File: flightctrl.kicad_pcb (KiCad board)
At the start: 1 copper layers, 51 parts, among them J1 USB_OTG, SW1 SW_SPST, SW10 ROTARY_ENCODER_SWITCH, SW2 SW_SPST, SW3 SW_SPST, SW4 SW_SPST, SW5 SW_SPDT_MSM, SW6 ROTARY_ENCODER_SWITCH, SW7 ROTARY_ENCODER_SWITCH, SW8 ROTARY_ENCODER_SWITCH, SW9 ROTARY_ENCODER_SWITCH, U1 ATMEGA328P-AU, Y1 12MHz

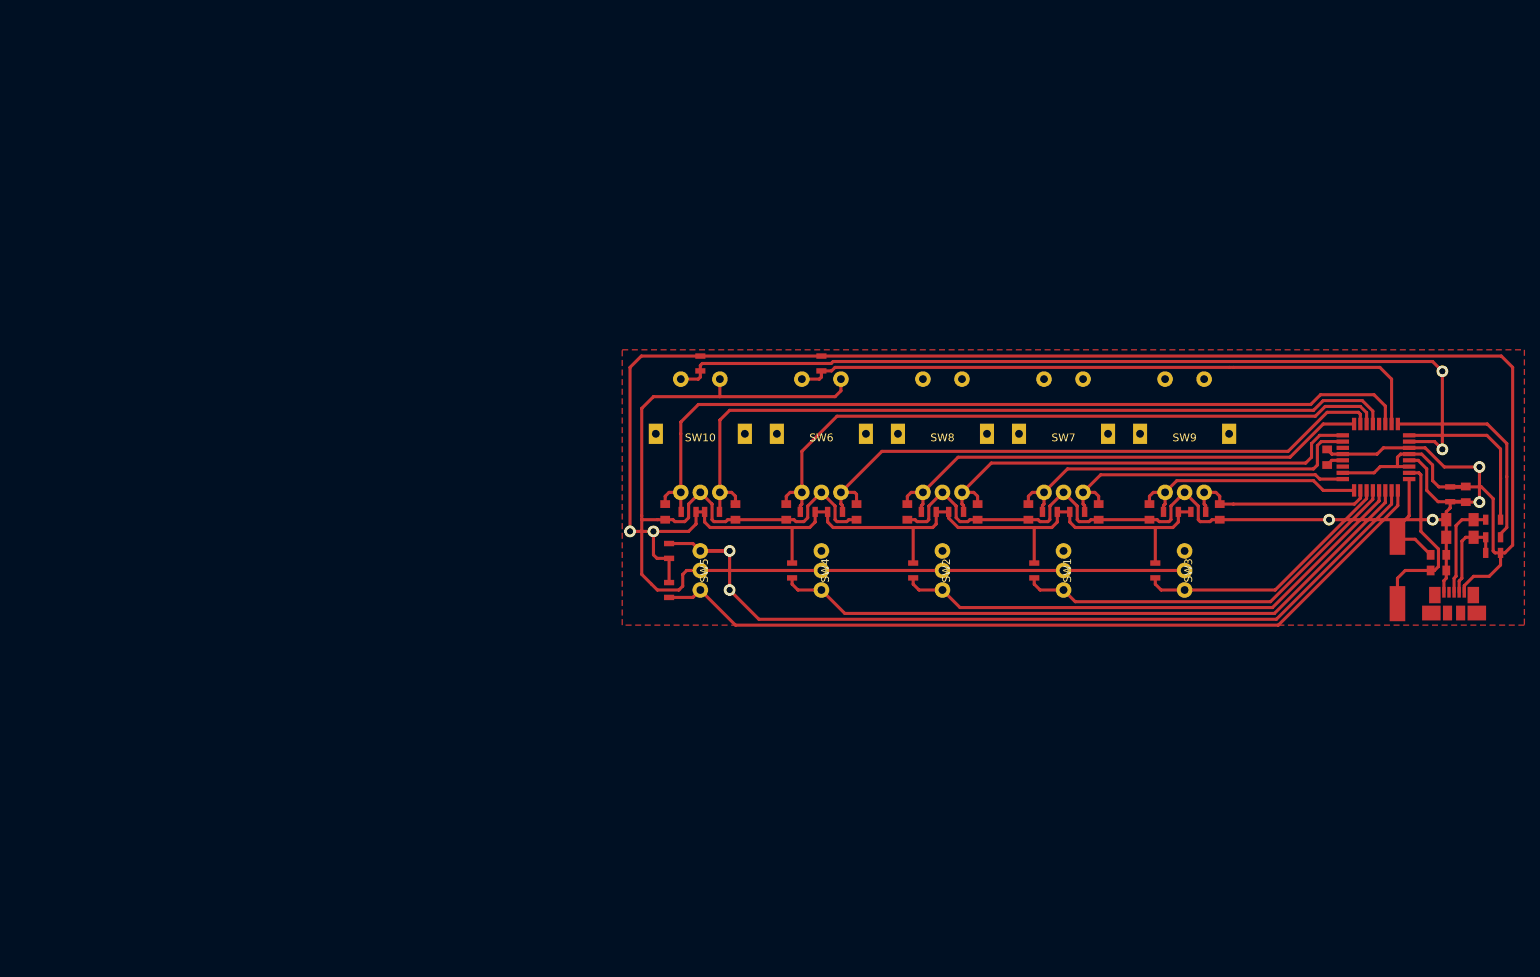
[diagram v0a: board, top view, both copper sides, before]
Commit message: create new hardware schematic and layout
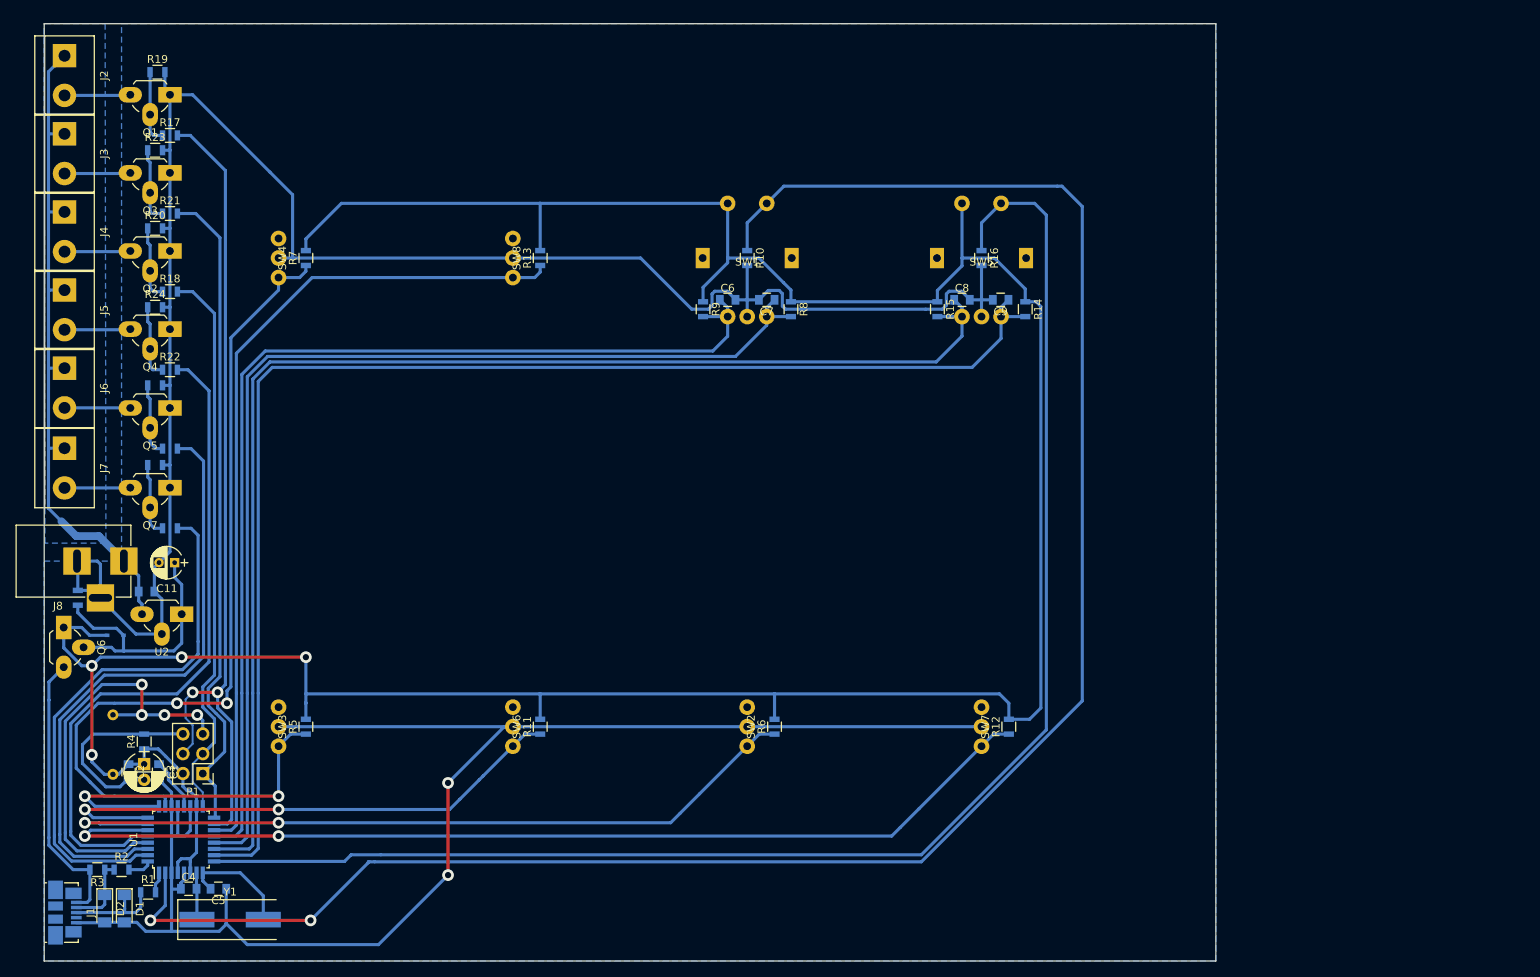
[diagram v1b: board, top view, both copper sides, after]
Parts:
- removed C12, C13, C14, C15: 100n, Capacitors_SMD:C_0805
- removed SW10, SW9: ROTARY_ENCODER_SWITCH, Button_Switch_THT:PEC11R-4xxxF-Sxxx
- added C1: 10µ, Capacitors_ThroughHole:CP_Radial_D5.0mm_P2.00mm, F.Cu at (52.8, 134.8)
- added D3: BAT20J, Diodes_SMD:D_SOD-323, B.Cu at (49.1, 118.3)
- added J2: CONN_01X02, Terminal_Blocks:TerminalBlock_bornier-2_P5.08mm, B.Cu at (42.6, 44.1)
- added J3: CONN_01X02, Terminal_Blocks:TerminalBlock_bornier-2_P5.08mm, B.Cu at (42.6, 54.1)
- added J4: CONN_01X02, Terminal_Blocks:TerminalBlock_bornier-2_P5.08mm, B.Cu at (42.6, 64.1)
- added J5: CONN_01X02, Terminal_Blocks:TerminalBlock_bornier-2_P5.08mm, B.Cu at (42.6, 74.1)
- added J6: CONN_01X02, Terminal_Blocks:TerminalBlock_bornier-2_P5.08mm, B.Cu at (42.6, 84.1)
- added J7: CONN_01X02, Terminal_Blocks:TerminalBlock_bornier-2_P5.08mm, B.Cu at (42.6, 94.3)
- added J8: BARREL_JACK, Connect:BARREL_JACK, F.Cu at (50.2, 108.8)
- added P1: CONN_02X03, Pin_Headers:Pin_Header_Straight_2x03_Pitch2.54mm, F.Cu at (60.3, 136.0)
- added Q1: 2N7000, TO_SOT_Packages_THT:TO-92_Rugged, B.Cu at (56.1, 49.1)
- added Q2: 2N7000, TO_SOT_Packages_THT:TO-92_Rugged, B.Cu at (56.1, 69.1)
- added Q3: 2N7000, TO_SOT_Packages_THT:TO-92_Rugged, B.Cu at (56.1, 59.1)
- added Q4: 2N7000, TO_SOT_Packages_THT:TO-92_Rugged, B.Cu at (56.1, 79.1)
- added Q5: 2N7000, TO_SOT_Packages_THT:TO-92_Rugged, B.Cu at (56.1, 89.2)
- added Q6: Q_PMOS_SGD, TO_SOT_Packages_THT:TO-92_Rugged, F.Cu at (42.5, 117.3)
- added Q7: 2N7000, TO_SOT_Packages_THT:TO-92_Rugged, B.Cu at (56.1, 99.4)
- added R23: 10k, Resistors_SMD:R_0805, B.Cu at (54.2, 56.2)
- added R24: 10k, Resistors_SMD:R_0805, B.Cu at (54.2, 76.3)
- added R25: 68, Resistors_SMD:R_0805, B.Cu at (56.1, 94.4)
- added R26: 10k, Resistors_SMD:R_0805, B.Cu at (44.3, 113.5)
- added R27: 10k, Resistors_SMD:R_0805, B.Cu at (54.2, 86.3)
- added R29: 68, Resistors_SMD:R_0805, B.Cu at (56.1, 104.6)
- added R30: 10k, Resistors_SMD:R_0805, B.Cu at (54.2, 96.5)
- added R31: 10k, Resistors_ThroughHole:R_Axial_DIN0204_L3.6mm_D1.6mm_P7.62mm_Horizontal, F.Cu at (48.8, 136.1)
- added U2: LM2931AZ-5.0, TO_SOT_Packages_THT:TO-92_Rugged, F.Cu at (57.6, 115.6)
- C10: value 100n -> 0.1u
- C11: value 100n -> 100u; footprint Capacitors_SMD:C_0805 -> Capacitors_ThroughHole:CP_Radial_D4.0mm_P2.00mm; moved to F.Cu
- R1, R17, R18, R21, R22: value 10k -> 68
- R2: value 56k -> 68
- R3: value 10k -> 1.5k
- R4: value 10k -> 56k
- R5, R6: value 68 -> 10k
- R7: value 1.5k -> 10k
- SW1: value SW_SPST -> ROTARY_ENCODER_SWITCH; footprint Button_Switch_THT:MKIP1PUM -> Button_Switch_THT:PEC11R-4xxxF-Sxxx
- SW5: value SW_SPDT_MSM -> ROTARY_ENCODER_SWITCH; footprint Button_Switch_THT:MKIP1PUM -> Button_Switch_THT:PEC11R-4xxxF-Sxxx
- SW6, SW7, SW8: value ROTARY_ENCODER_SWITCH -> SW_SPST; footprint Button_Switch_THT:PEC11R-4xxxF-Sxxx -> Button_Switch_THT:MKIP1PUM
- moved J1 182.2 mm to (42.6, 153.8), turned to 270 degrees
- moved D2 179.9 mm to (47.8, 153.3), turned to 270 degrees
- moved D1 178.1 mm to (50.2, 153.3), turned to 270 degrees
- moved R2 176.8 mm to (49.9, 148.3), turned to 0 degrees
- moved C2 174.9 mm to (50.8, 135.8)
- moved C4 165.1 mm to (58.5, 150.8), turned to 0 degrees
- moved C5 161.9 mm to (62.3, 150.8)
- moved U1 160.6 mm to (57.5, 144.4), turned to 90 degrees
- moved R7 156.6 mm to (73.5, 70.0), turned to 90 degrees
- moved Y1 156.0 mm to (63.8, 154.7), turned to 0 degrees
- moved C3 154.9 mm to (54.7, 135.8), turned to 270 degrees
- moved R5 154.3 mm to (73.5, 130.0), turned to 90 degrees
- moved R4 131.3 mm to (52.8, 131.9)
- moved R18 131.2 mm to (56.1, 74.3), turned to 0 degrees
- moved C11 125.0 mm to (56.7, 109.0), turned to 180 degrees
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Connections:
- C10 pad 1: SW1_A -> +12V
- C11 pad 1: SW3_A -> Net-(C11-Pad1)
- C6 pad 1: SW2_A -> SW7_A
- C7 pad 1: SW4_A -> SW7_B
- C8 pad 1: SW2_B -> SW8_A
- C9 pad 1: SW4_B -> SW8_B
- J1 pad 1: +5V -> Net-(J1-Pad1)
- J1 pad 4: Net-(J1-Pad4) -> (no net)
- R1 pad 1: SW6 -> Net-(D1-Pad1)
- R1 pad 2: +5V -> USB_DP
- R10 pad 1: +5V -> SW7_C
- R10 pad 2: SW2_B -> GND
- R11 pad 1: +5V -> SW2
- R11 pad 2: SW4_B -> +5V
- R12 pad 1: +5V -> SW4
- R12 pad 2: SW2_A -> +5V
- R13 pad 1: +5V -> SW6
- R13 pad 2: SW4_A -> +5V
- R14 pad 2: SW1_B -> SW8_B
- R15 pad 2: SW3_B -> SW8_A
- R16 pad 1: +5V -> SW8_C
- R16 pad 2: SW5_B -> GND
- R17 pad 1: +5V -> Net-(Q1-Pad2)
- R17 pad 2: SW1_A -> OUT1
- R18 pad 1: +5V -> Net-(Q2-Pad2)
- R18 pad 2: SW3_A -> OUT3
- R19 pad 1: +5V -> Net-(Q1-Pad2)
- R19 pad 2: SW5_A -> GND
- R2 pad 1: +5V -> Net-(D2-Pad1)
- R2 pad 2: GND -> USB_DM
- R20 pad 1: SW10b -> Net-(Q2-Pad2)
- R20 pad 2: +5V -> GND
- R21 pad 1: +5V -> Net-(Q3-Pad2)
- R21 pad 2: SW4_C -> OUT2
- R22 pad 1: +5V -> Net-(Q4-Pad2)
- R22 pad 2: SW5_C -> OUT4
- R3 pad 1: SW7 -> Net-(D2-Pad1)
- R3 pad 2: +5V -> Net-(J1-Pad1)
- R4 pad 1: SW8 -> +5V
- R4 pad 2: +5V -> GND
- R5 pad 1: Net-(D1-Pad1) -> SW1
- R5 pad 2: USB_DP -> +5V
- R6 pad 1: Net-(D2-Pad1) -> SW3
- R6 pad 2: USB_DM -> +5V
- R7 pad 1: Net-(D2-Pad1) -> SW5
- R8 pad 1: SW9 -> +5V
- R8 pad 2: +5V -> SW7_B
- R9 pad 1: SW10a -> +5V
- R9 pad 2: +5V -> SW7_A
- SW1 pad 1: SW6 -> SW7_A
- SW1 pad 3: (no net) -> SW7_B
- SW2 pad 1: SW7 -> SW3
- SW3 pad 1: SW8 -> SW1
- SW4 pad 1: SW9 -> SW5
- SW5 pad 1: SW10b -> SW8_A
- SW5 pad 3: SW10a -> SW8_B
- SW6 pad 1: SW4_A -> SW2
- SW6 pad 3: SW4_B -> (no net)
- SW7 pad 1: SW2_A -> SW4
- SW7 pad 3: SW2_B -> (no net)
- SW8 pad 1: SW1_A -> SW6
- SW8 pad 3: SW1_B -> (no net)
- U1 pad 10: SW10a -> SW8_B
- U1 pad 11: SW9 -> SW8_A
- U1 pad 12: SW7 -> SW7_B
- U1 pad 13: SW6 -> SW7_A
- U1 pad 14: SW8 -> SW6
- U1 pad 15: SW3_B -> OUT1
- U1 pad 16: SW3_A -> OUT2
- U1 pad 17: SW2_B -> OUT3
- U1 pad 19: Net-(U1-Pad19) -> GND
- U1 pad 2: SW5_C -> SW7_C
- U1 pad 22: Net-(U1-Pad22) -> GND
- U1 pad 23: SW2_A -> SW5
- U1 pad 24: SW1_B -> SW1
- U1 pad 25: SW1_A -> SW2
- U1 pad 26: SW4_B -> SW3
- U1 pad 27: SW4_A -> SW4
- U1 pad 28: SW5_B -> OUT4
- U1 pad 30: SW5_A -> OUT5
- U1 pad 31: SW4_C -> OUT6
- U1 pad 9: SW10b -> SW8_C
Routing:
- net SW7_C: track 0.00 -> 250.9 mm, vias 0 -> 2
- net SW8_C: track 0.00 -> 192.9 mm
- net GND: track 297.2 -> 478.8 mm, vias 4 -> 2
- net SW8_B: track 0.00 -> 171.6 mm
- net SW8_A: track 0.00 -> 166.1 mm
- net SW7_B: track 0.00 -> 139.5 mm
- net SW7_A: track 0.00 -> 134.6 mm
- net SW4: track 0.00 -> 132.1 mm, vias 0 -> 2
- net SW5_C: track 114.5 -> 0.00 mm, vias 2 -> 0
- net SW5_A: track 109.3 -> 0.00 mm
- net SW10a: track 107.3 -> 0.00 mm, vias 2 -> 0
- net OUT1: track 0.00 -> 107.1 mm, vias 0 -> 2
- net SW10b: track 103.8 -> 0.00 mm
- net SW5_B: track 102.4 -> 0.00 mm
- net SW5: track 0.00 -> 101.8 mm, vias 0 -> 2
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- added copper zone on B.Cu, net +12V
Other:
- board outline added: 150 x 120 mm
- copper layers 1 -> 2

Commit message: minors
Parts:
- moved J7 1.46 mm to (43.5, 95.5)
- moved J2 1.42 mm to (43.5, 43.0)
- moved J6 1.27 mm to (43.5, 85.0)
- moved J3 1.08 mm to (43.5, 53.5)
- moved J5 0.98 mm to (43.5, 74.5)
- moved J4 0.91 mm to (43.5, 64.0)
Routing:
- net +12V: track 89.8 -> 15.1 mm
- net /Output/O3: track 8.25 -> 7.53 mm
- net /Output/O4: track 8.25 -> 7.72 mm
- net /Output/O2: track 8.25 -> 7.74 mm

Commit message: minors
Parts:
- moved J2 0.50 mm to (44.0, 43.0)
- moved J3 0.50 mm to (44.0, 53.5)
- moved J4 0.50 mm to (44.0, 64.0)
- moved J5 0.50 mm to (44.0, 74.5)
- moved J6 0.50 mm to (44.0, 85.0)
- moved J7 0.50 mm to (44.0, 95.5)
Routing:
- net /Output/O5: track 7.88 -> 7.38 mm
- net /Output/O4: track 7.72 -> 7.22 mm
- net /Output/O3: track 7.53 -> 7.03 mm
- net /Output/O2: track 7.74 -> 7.24 mm
- net /Output/O1: track 7.94 -> 7.44 mm
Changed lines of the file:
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@@
   (general
     (thickness 1.6)
-    (drawings 4)
+    (drawings 6)
     (tracks 588)
     (zones 0)
@@
   )
   (setup
-    (last_trace_width 0.4)
+    (last_trace_width 1)
     (user_trace_width 0.4)
     (user_trace_width 1)
@@
   )
   (module Terminal_Blocks:TerminalBlock_bornier-2_P5.08mm (layer B.Cu)
-    (at 43.5 53.5 270)
+    (at 44 53.5 270)
     (descr "simple 2-pin terminal block, pitch 5.08mm, revamped version of bornier2")
     (tags "terminal block bornier2")
@@
   )
   (module Terminal_Blocks:TerminalBlock_bornier-2_P5.08mm (layer B.Cu)
-    (at 43.5 95.5 270)
+    (at 44 95.5 270)
     (descr "simple 2-pin terminal block, pitch 5.08mm, revamped version of bornier2")
     (tags "terminal block bornier2")
@@
   )
   (module Terminal_Blocks:TerminalBlock_bornier-2_P5.08mm (layer B.Cu)
-    (at 43.5 43 270)
+    (at 44 43 270)
     (descr "simple 2-pin terminal block, pitch 5.08mm, revamped version of bornier2")
     (tags "terminal block bornier2")
@@
   )
   (module Terminal_Blocks:TerminalBlock_bornier-2_P5.08mm (layer B.Cu)
-    (at 43.5 64 270)
+    (at 44 64 270)
     (descr "simple 2-pin terminal block, pitch 5.08mm, revamped version of bornier2")
     (tags "terminal block bornier2")
@@
   )
   (module Terminal_Blocks:TerminalBlock_bornier-2_P5.08mm (layer B.Cu)
-    (at 43.5 74.5 270)
+    (at 44 74.5 270)
     (descr "simple 2-pin terminal block, pitch 5.08mm, revamped version of bornier2")
     (tags "terminal block bornier2")
@@
   )
   (module Terminal_Blocks:TerminalBlock_bornier-2_P5.08mm (layer B.Cu)
-    (at 43.5 85 270)
+    (at 44 85 270)
     (descr "simple 2-pin terminal block, pitch 5.08mm, revamped version of bornier2")
     (tags "terminal block bornier2")
@@
     )
   )
+  (dimension 120 (width 0.3) (layer Cmts.User)
+    (gr_text "120,000 mm" (at 198.85 100 270) (layer Cmts.User)
+      (effects (font (size 1.5 1.5) (thickness 0.3)))
+    )
+    (feature1 (pts (xy 190 160) (xy 200.2 160)))
+    (feature2 (pts (xy 190 40) (xy 200.2 40)))
+    (crossbar (pts (xy 197.5 40) (xy 197.5 160)))
+    (arrow1a (pts (xy 197.5 160) (xy 196.913579 158.873496)))
+    (arrow1b (pts (xy 197.5 160) (xy 198.086421 158.873496)))
+    (arrow2a (pts (xy 197.5 40) (xy 196.913579 41.126504)))
+    (arrow2b (pts (xy 197.5 40) (xy 198.086421 41.126504)))
+  )
+  (dimension 150 (width 0.3) (layer Cmts.User)
+    (gr_text "150,000 mm" (at 115 33.65) (layer Cmts.User)
+      (effects (font (size 1.5 1.5) (thickness 0.3)))
+    )
+    (feature1 (pts (xy 190 40) (xy 190 32.3)))
+    (feature2 (pts (xy 40 40) (xy 40 32.3)))
+    (crossbar (pts (xy 40 35) (xy 190 35)))
+    (arrow1a (pts (xy 190 35) (xy 188.873496 35.586421)))
+    (arrow1b (pts (xy 190 35) (xy 188.873496 34.413579)))
+    (arrow2a (pts (xy 40 35) (xy 41.126504 35.586421)))
+    (arrow2b (pts (xy 40 35) (xy 41.126504 34.413579)))
+  )
   (gr_line (start 40 160) (end 190 160) (angle 90) (layer Edge.Cuts) (width 0.1))
   (gr_line (start 190 40) (end 190 160) (angle 90) (layer Edge.Cuts) (width 0.1))
@@
   (segment (start 51.35 144.05) (end 50.2 145.2) (width 0.4) (layer B.Cu) (net 31))
   (segment (start 61.1 121.7) (end 61.1 87) (width 0.4) (layer B.Cu) (net 31))
-  (segment (start 45.62132 48.08) (end 46.64132 49.1) (width 0.4) (layer B.Cu) (net 32))
-  (segment (start 43.5 48.08) (end 45.62132 48.08) (width 0.4) (layer B.Cu) (net 32))
-  (segment (start 46.64132 49.1) (end 51.02 49.1) (width 0.4) (layer B.Cu) (net 32))
-  (segment (start 46.58 58.58) (end 47.1 59.1) (width 0.4) (layer B.Cu) (net 33))
-  (segment (start 47.1 59.1) (end 51.02 59.1) (width 0.4) (layer B.Cu) (net 33))
-  (segment (start 43.5 58.58) (end 46.58 58.58) (width 0.4) (layer B.Cu) (net 33))
-  (segment (start 43.5 69.08) (end 51 69.08) (width 0.4) (layer B.Cu) (net 34))
-  (segment (start 51 69.08) (end 51.02 69.1) (width 0.4) (layer B.Cu) (net 34))
-  (segment (start 46.42 79.58) (end 46.9 79.1) (width 0.4) (layer B.Cu) (net 35))
-  (segment (start 46.9 79.1) (end 51.02 79.1) (width 0.4) (layer B.Cu) (net 35))
-  (segment (start 43.5 79.58) (end 46.42 79.58) (width 0.4) (layer B.Cu) (net 35))
-  (segment (start 45.92 90.08) (end 46.8 89.2) (width 0.4) (layer B.Cu) (net 36))
-  (segment (start 46.8 89.2) (end 51.02 89.2) (width 0.4) (layer B.Cu) (net 36))
-  (segment (start 43.5 90.08) (end 45.92 90.08) (width 0.4) (layer B.Cu) (net 36))
-  (segment (start 46.42 100.58) (end 47.6 99.4) (width 0.4) (layer B.Cu) (net 37))
-  (segment (start 47.6 99.4) (end 51.02 99.4) (width 0.4) (layer B.Cu) (net 37))
-  (segment (start 43.5 100.58) (end 46.42 100.58) (width 0.4) (layer B.Cu) (net 37))
+  (segment (start 47.08 48.08) (end 48.1 49.1) (width 1) (layer B.Cu) (net 32))
+  (segment (start 48.1 49.1) (end 51.02 49.1) (width 1) (layer B.Cu) (net 32))
+  (segment (start 44 48.08) (end 47.08 48.08) (width 1) (layer B.Cu) (net 32))
+  (segment (start 46.12132 58.58) (end 46.64132 59.1) (width 1) (layer B.Cu) (net 33))
+  (segment (start 44 58.58) (end 46.12132 58.58) (width 1) (layer B.Cu) (net 33))
+  (segment (start 46.64132 59.1) (end 51.02 59.1) (width 1) (layer B.Cu) (net 33))
+  (segment (start 44 69.08) (end 51 69.08) (width 1) (layer B.Cu) (net 34))
+  (segment (start 51 69.08) (end 51.02 69.1) (width 1) (layer B.Cu) (net 34))
+  (segment (start 46.12132 79.58) (end 46.60132 79.1) (width 1) (layer B.Cu) (net 35))
+  (segment (start 44 79.58) (end 46.12132 79.58) (width 1) (layer B.Cu) (net 35))
+  (segment (start 46.60132 79.1) (end 51.02 79.1) (width 1) (layer B.Cu) (net 35))
+  (segment (start 46.12132 90.08) (end 47.00132 89.2) (width 1) (layer B.Cu) (net 36))
+  (segment (start 44 90.08) (end 46.12132 90.08) (width 1) (layer B.Cu) (net 36))
+  (segment (start 47.00132 89.2) (end 51.02 89.2) (width 1) (layer B.Cu) (net 36))
+  (segment (start 46.12132 100.58) (end 47.30132 99.4) (width 1) (layer B.Cu) (net 37))
+  (segment (start 44 100.58) (end 46.12132 100.58) (width 1) (layer B.Cu) (net 37))
+  (segment (start 47.30132 99.4) (end 51.02 99.4) (width 1) (layer B.Cu) (net 37))
   (segment (start 55.15 94.4) (end 54.3 94.4) (width 0.4) (layer B.Cu) (net 38))
   (segment (start 53.56 93.66) (end 53.56 91.74) (width 0.4) (layer B.Cu) (net 38))
@@
     (polygon
       (pts
-        (xy 190 160) (xy 40 160) (xy 40 108.8) (xy 49.9 108.8) (xy 49.9 40)
+        (xy 190 160) (xy 40 160) (xy 40 108) (xy 49.9 108) (xy 49.9 40)
         (xy 190 40)
       )
